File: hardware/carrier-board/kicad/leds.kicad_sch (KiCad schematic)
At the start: 0 parts

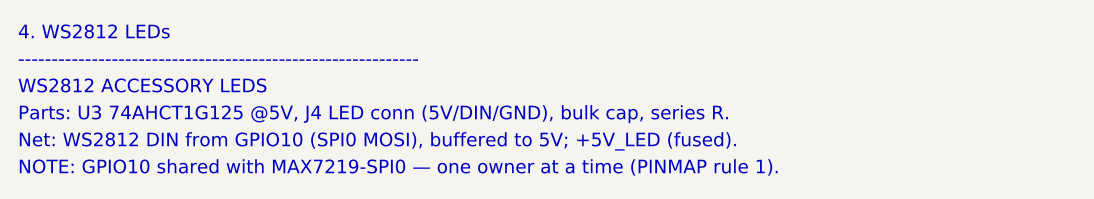
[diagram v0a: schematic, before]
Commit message: Carrier docs + KiCad plan: full two-brain pass (CM5 HUB75 + RP2354B I/O)
Propagate the two-brain architecture across the whole doc set and KiCad plan:
- REQUIREMENTS: restructured M1-M12 (CM5 HUB75; RP2354B core/MAX7219/WS2812/
  sensors/buttons/servos; USB selector + standalone program port); N-list reworked.
- POWER: add +V_SERVO and +3V3_RP rails, servo current budget, updated worked
  total + protection; sensors now on +3V3_RP not CM5 3V3.
- CONNECTORS: J3 re-sourced to RP2354B SPI0, J4 4 WS2812 zones, J5 +SENS_INT,
  J6 BTN1..10, add J12 USB-C, J20-J27 servos, SW1 USB selector, SWD/UART hdrs;
  drop JP1/JP2; fans presented as RP2354B-default-or-CM5 (decision flagged).
- BOM: add RP2354B core, '125/'245 (RP side), USB mux/USB-C/ESD, servo headers,
  +3V3_RP reg; fix '125 double-count and stale HUB75/MAX7219-shared-buffer/JP1.
- MULTI-BACKEND: HUB75+MAX7219 now simultaneous (different brains); firmware
  CompositePanelOutput is the sole remaining blocker.
- IO-EXPANSION: RP2354B is the primary I/O backbone; I2C expanders secondary.
- kicad: 11-sheet plan, stable UUIDs, generator skips populated face_buffer.
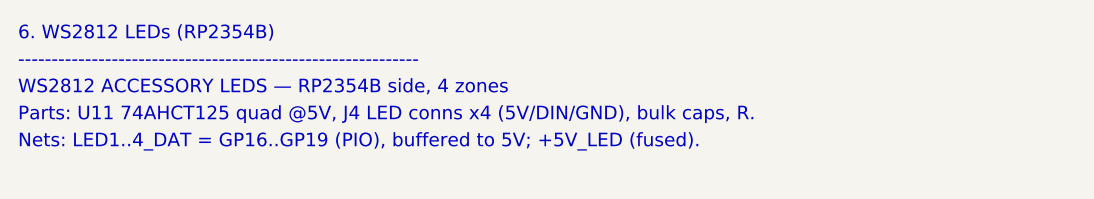
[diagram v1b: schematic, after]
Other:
- note added: "6. WS2812 LEDs (RP2354B)"
- note added: "Nets: LED1..4_DAT = GP16..GP19 (PIO), buffered to 5V; +5V_LED (fused)."
- note added: "Parts: U11 74AHCT125 quad @5V, J4 LED conns x4 (5V/DIN/GND), bulk caps, R."
- note added: "WS2812 ACCESSORY LEDS — RP2354B side, 4 zones"
- note removed: "4. WS2812 LEDs"
- note removed: "NOTE: GPIO10 shared with MAX7219-SPI0 — one owner at a time (PINMAP rule 1)."
- note removed: "Net: WS2812 DIN from GPIO10 (SPI0 MOSI), buffered to 5V; +5V_LED (fused)."
- note removed: "Parts: U3 74AHCT1G125 @5V, J4 LED conn (5V/DIN/GND), bulk cap, series R."
- note removed: "WS2812 ACCESSORY LEDS"
- title: ProtoHUD Carrier — 4. WS2812 LEDs -> ProtoHUD Carrier — 6. WS2812 LEDs (RP2354B)
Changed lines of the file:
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@@
   (paper "A3")
   (title_block
-    (title "ProtoHUD Carrier — 4. WS2812 LEDs")
+    (title "ProtoHUD Carrier — 6. WS2812 LEDs (RP2354B)")
     (rev "A")
     (company "ProtoHUD")
   )
-  (text "4. WS2812 LEDs" (at 25.4 25.40 0) (effects (font (size 1.5 1.5)) (justify left bottom)))
+  (text "6. WS2812 LEDs (RP2354B)" (at 25.4 25.40 0) (effects (font (size 1.5 1.5)) (justify left bottom)))
   (text "------------------------------------------------------------" (at 25.4 28.40 0) (effects (font (size 1.5 1.5)) (justify left bottom)))
-  (text "WS2812 ACCESSORY LEDS" (at 25.4 31.40 0) (effects (font (size 1.5 1.5)) (justify left bottom)))
-  (text "Parts: U3 74AHCT1G125 @5V, J4 LED conn (5V/DIN/GND), bulk cap, series R." (at 25.4 34.40 0) (effects (font (size 1.5 1.5)) (justify left bottom)))
-  (text "Net: WS2812 DIN from GPIO10 (SPI0 MOSI), buffered to 5V; +5V_LED (fused)." (at 25.4 37.40 0) (effects (font (size 1.5 1.5)) (justify left bottom)))
-  (text "NOTE: GPIO10 shared with MAX7219-SPI0 — one owner at a time (PINMAP rule 1)." (at 25.4 40.40 0) (effects (font (size 1.5 1.5)) (justify left bottom)))
+  (text "WS2812 ACCESSORY LEDS — RP2354B side, 4 zones" (at 25.4 31.40 0) (effects (font (size 1.5 1.5)) (justify left bottom)))
+  (text "Parts: U11 74AHCT125 quad @5V, J4 LED conns x4 (5V/DIN/GND), bulk caps, R." (at 25.4 34.40 0) (effects (font (size 1.5 1.5)) (justify left bottom)))
+  (text "Nets: LED1..4_DAT = GP16..GP19 (PIO), buffered to 5V; +5V_LED (fused)." (at 25.4 37.40 0) (effects (font (size 1.5 1.5)) (justify left bottom)))
   (sheet_instances
     (path "/" (page "1"))

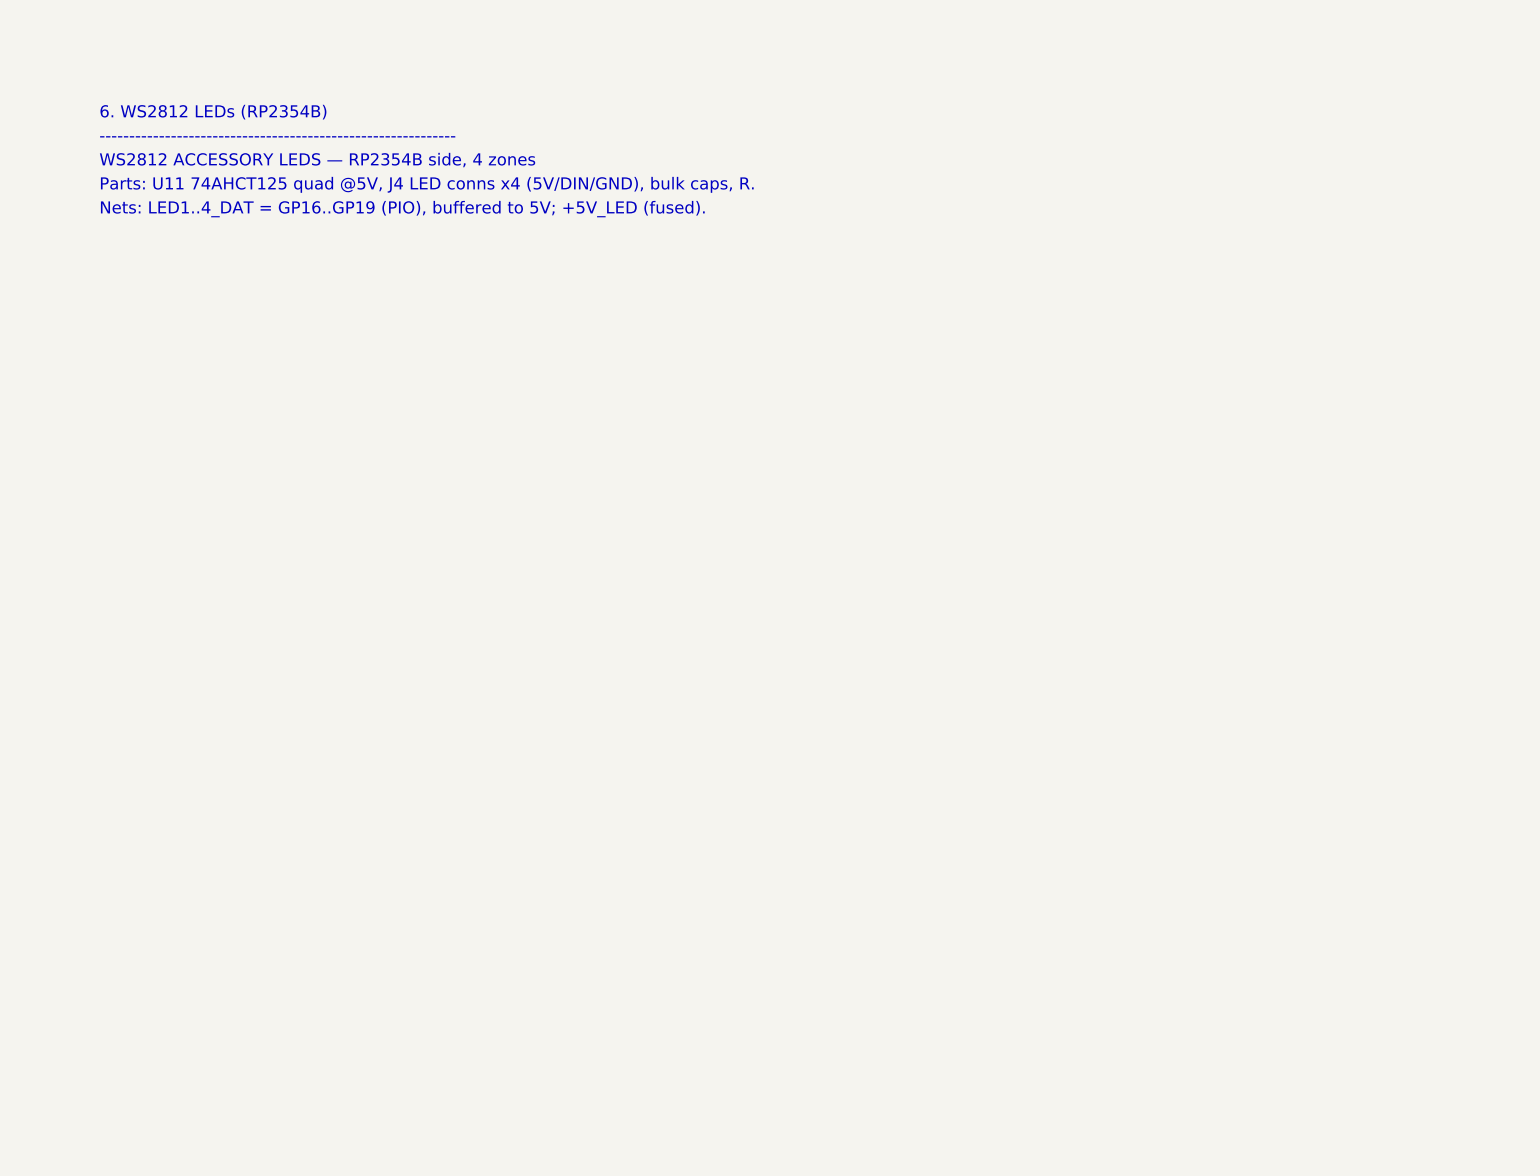
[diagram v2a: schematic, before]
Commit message: Carrier KiCad: populate all 11 schematic sheets
Replace populate_face_buffer.py with populate_sheets.py: one generator that
emits all 11 populated sub-sheets reusing the KiCad-9 format proven by the
face_buffer proof. Shared symbol library + generic box-symbol builder; condensed
CM5 (2x DF40-100) and RP2354B (QFN-80) symbols showing only used pins.

Connectivity by net labels (global for rails + cross-sheet nets: GPIOxx HUB75,
MX_*, LED*_DAT, SRV*, BTN*, *_USB_*; local within-sheet). Sheets: power
(protection + rails + AP2112 +3V3_RP), cm5 (HUB75 out + fan MOSFETs + RP ctrl),
face_buffer, rp2354_io (RP2354B + xtal + SW1/J12 + ESD + SWD), rp2354_face
(U10->J3), leds (U11 quad ->J4a-d), sensors_i2c (pull-ups+J5+STEMMA),
servos (J20-27 + rail), gpio_buttons (J6), usb (USB2514B hub + uplink),
cameras_display (CSI FFC + HDMI).

Verified: all sheets paren-balanced, every used lib_id defined, all instance
paths match sheet UUIDs, root<->sub-sheet UUID linkage intact. generate_skeleton.py
now lists all sheets POPULATED (writes only root+project). Not yet opened in
KiCad here -- expect ERC warnings (PWR_FLAG, unconnected pins) to clean.
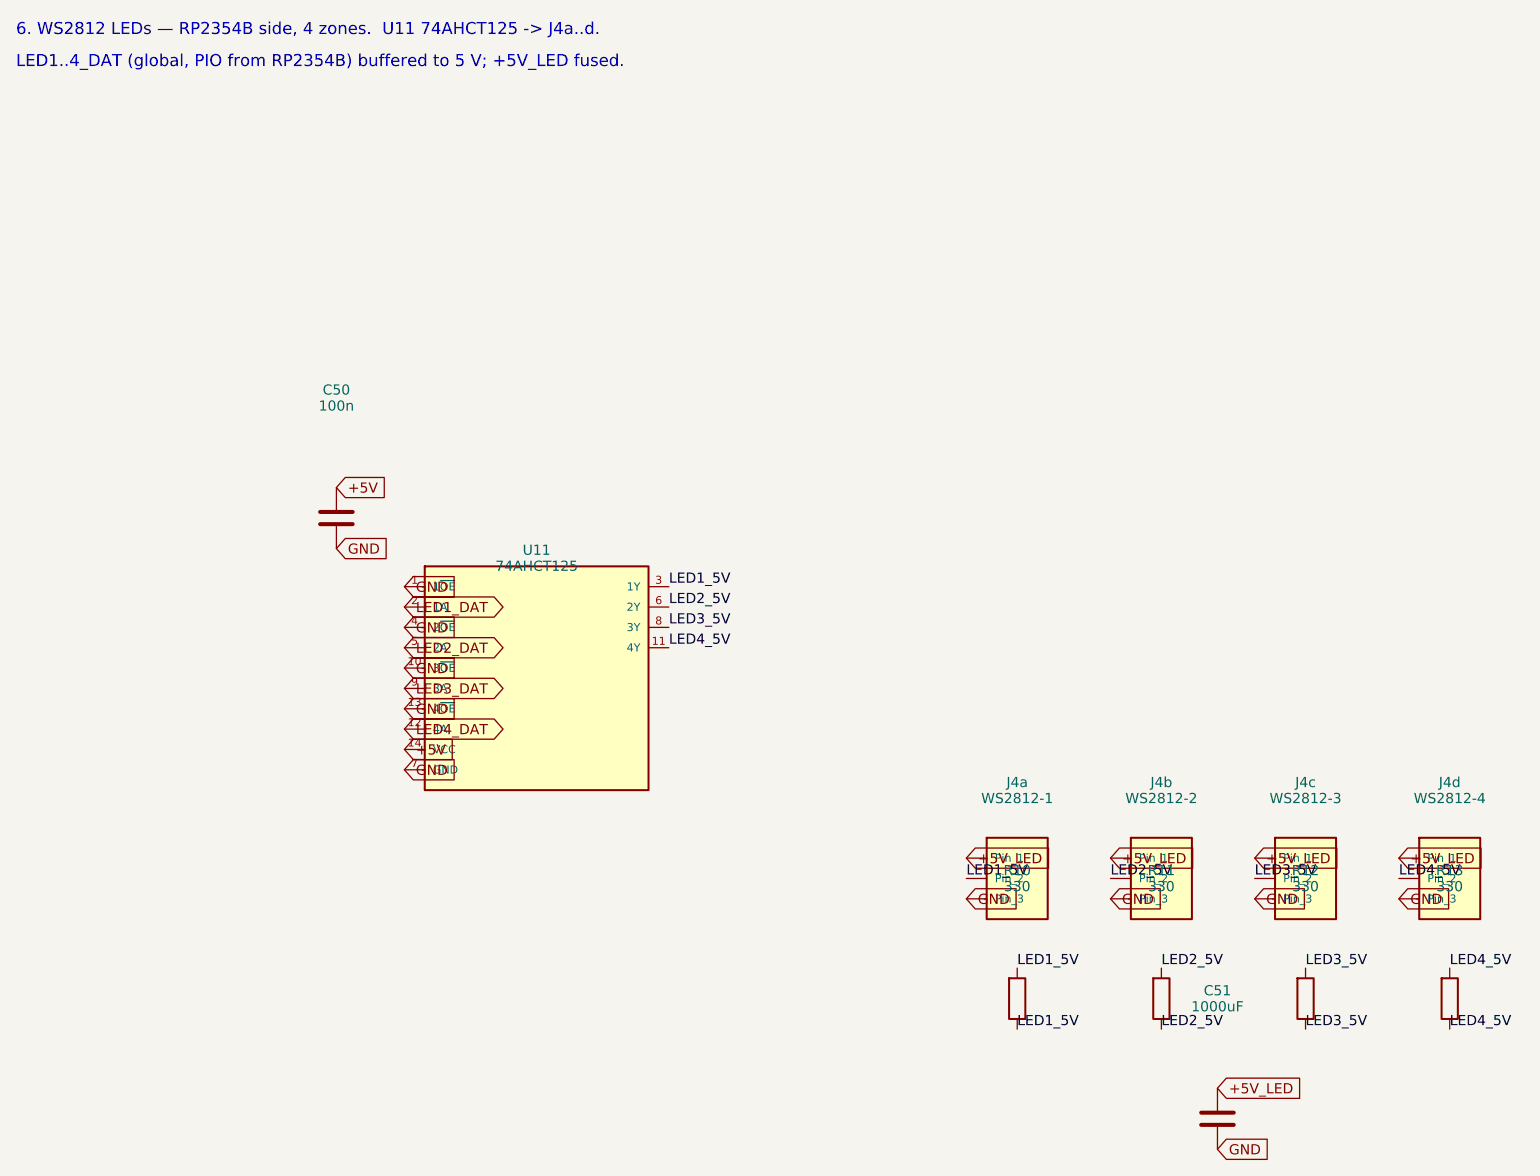
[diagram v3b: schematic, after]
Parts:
- added C50: 100n, symbol Device:C
- added C51: 1000uF, symbol Device:C
- added J4a: WS2812-1, symbol Connector_Generic:Conn_01x03
- added J4b: WS2812-2, symbol Connector_Generic:Conn_01x03
- added J4c: WS2812-3, symbol Connector_Generic:Conn_01x03
- added J4d: WS2812-4, symbol Connector_Generic:Conn_01x03
- added R10, R11, R12, R13: 330, symbol Device:R
- added U11: 74AHCT125, symbol 74xx:74AHCT125
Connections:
- new net +5V: C50.1, U11.14 (VCC)
- new net +5V_LED: C51.1, J4a.1 (Pin_1), J4b.1 (Pin_1), J4c.1 (Pin_1), J4d.1 (Pin_1)
- new net GND: C50.2, C51.2, J4a.3 (Pin_3), J4b.3 (Pin_3), J4c.3 (Pin_3), J4d.3 (Pin_3), U11.1 (1~{OE}), U11.10 (3~{OE}), U11.13 (4~{OE}), U11.4 (2~{OE}), U11.7 (GND)
- new net LED1_5V: J4a.2 (Pin_2), R10.1, R10.2, U11.3 (1Y)
- new net LED1_DAT: U11.2 (1A)
- new net LED2_5V: J4b.2 (Pin_2), R11.1, R11.2, U11.6 (2Y)
- new net LED2_DAT: U11.5 (2A)
- new net LED3_5V: J4c.2 (Pin_2), R12.1, R12.2, U11.8 (3Y)
- new net LED3_DAT: U11.9 (3A)
- new net LED4_5V: J4d.2 (Pin_2), R13.1, R13.2, U11.11 (4Y)
- new net LED4_DAT: U11.12 (4A)
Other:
- note added: "6. WS2812 LEDs — RP2354B side, 4 zones. U11 74AHCT125 -> J4a..d."
- note added: "LED1..4_DAT (global, PIO from RP2354B) buffered to 5 V; +5V_LED fused."
- note removed: "------------------------------------------------------------"
- note removed: "6. WS2812 LEDs (RP2354B)"
- note removed: "Nets: LED1..4_DAT = GP16..GP19 (PIO), buffered to 5V; +5V_LED (fused)."
- note removed: "Parts: U11 74AHCT125 quad @5V, J4 LED conns x4 (5V/DIN/GND), bulk caps, R."
- note removed: "WS2812 ACCESSORY LEDS — RP2354B side, 4 zones"
